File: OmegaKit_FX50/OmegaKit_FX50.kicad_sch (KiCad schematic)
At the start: 25 parts, among them U1 ESP32-DEVKIT-V1, U2 AMS1117-3.3

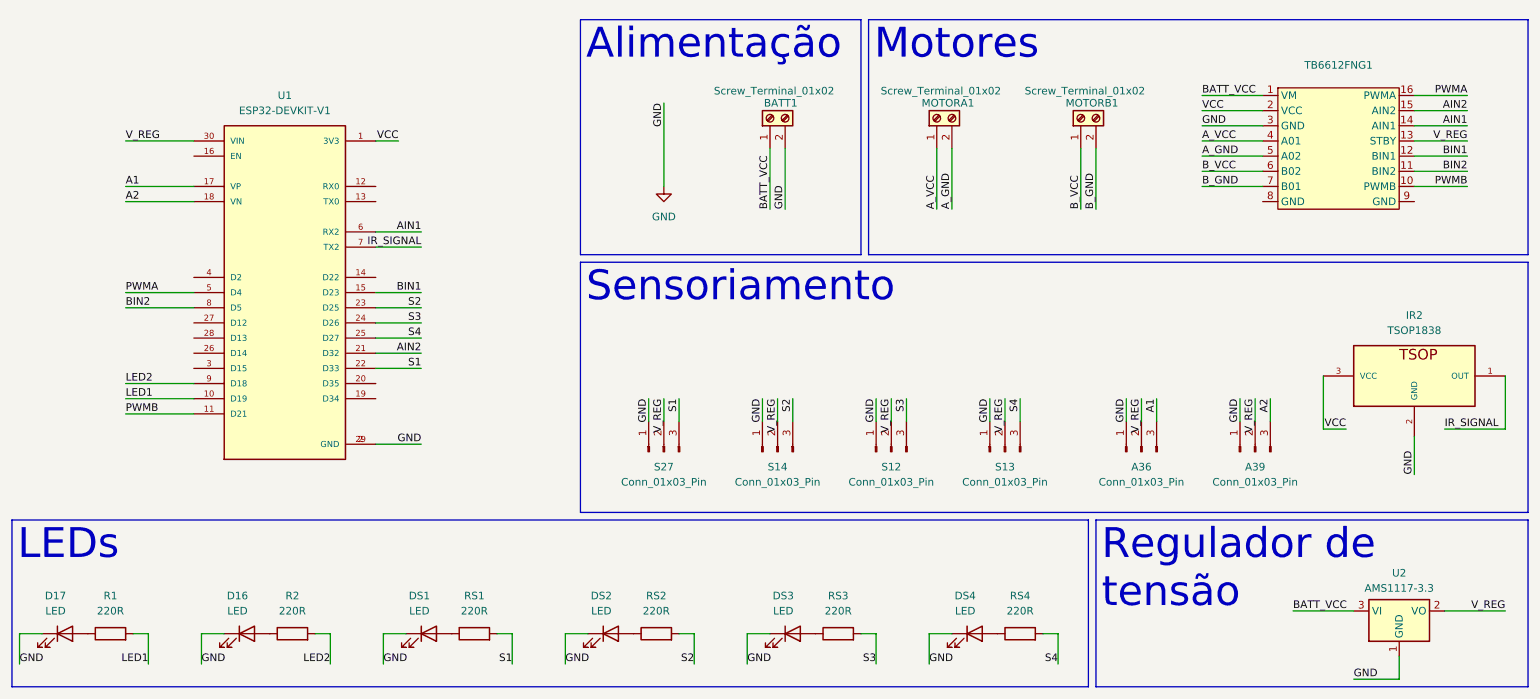
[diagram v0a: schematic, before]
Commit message: Ajustes regulador de tensão + switch e capacitor + não usar pinoGPIO12
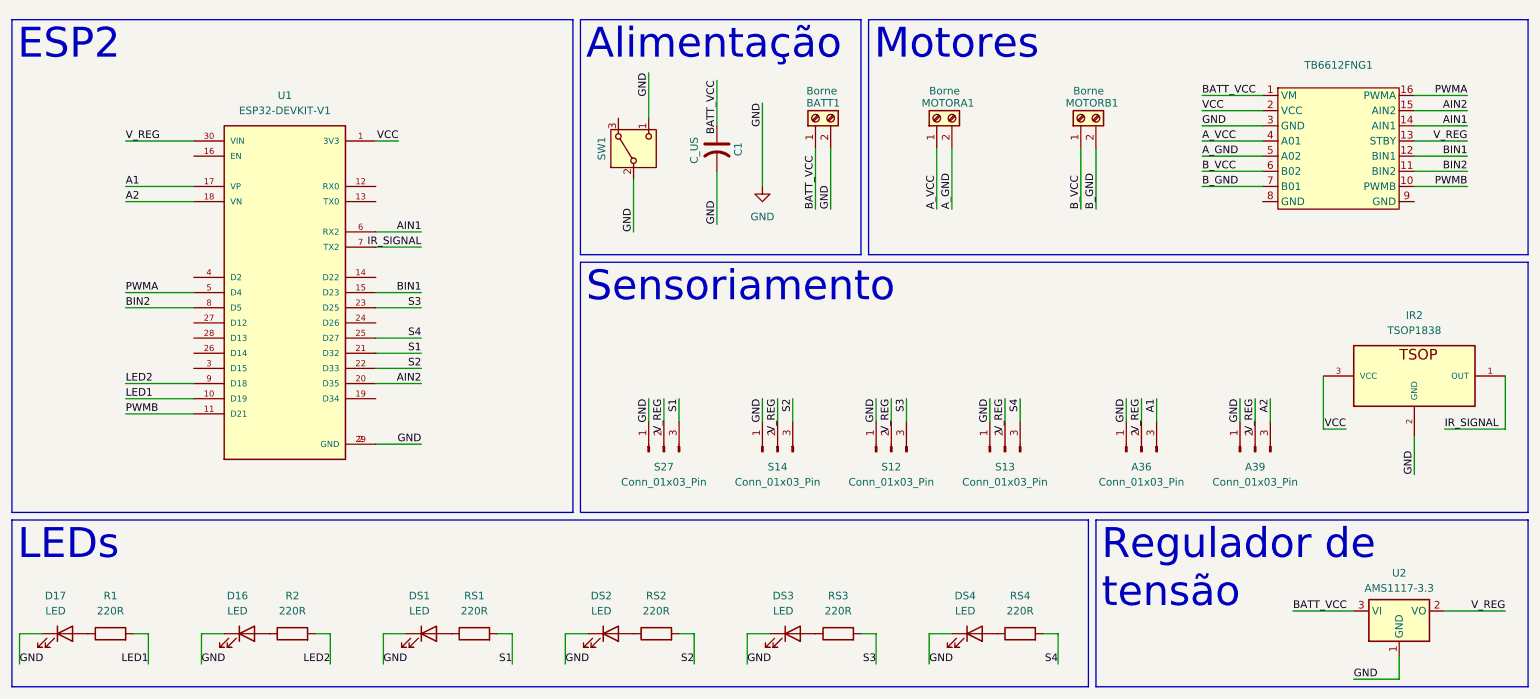
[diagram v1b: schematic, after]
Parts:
- added C1: C_US, Capacitor_THT:C_Radial_D5.0mm_H5.0mm_P2.00mm, symbol Device:C_US
- added SW1: SW_Nidec_CAS-120A1, Button_Switch_SMD:Nidec_Copal_CAS-120A, symbol Switch:SW_Nidec_CAS-120A1
- BATT1, MOTORA1, MOTORB1: value Screw_Terminal_01x02 -> Borne
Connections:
- net AIN2: now also U1.20 (D35); no longer U1.21 (D32)
- net BATT_VCC: now also C1.1
- net GND: now also C1.2, SW1.1 (C), SW1.2 (B)
- net S1: now also U1.21 (D32); no longer U1.22 (D33)
- net S2: now also U1.22 (D33); no longer U1.23 (D25)
- net S3: now also U1.23 (D25); no longer U1.24 (D26)
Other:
- moved on the sheet: BATT1
